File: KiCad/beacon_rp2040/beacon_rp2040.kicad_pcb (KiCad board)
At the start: 2 copper layers, 1 part, among them U1 RP2040-ZERO

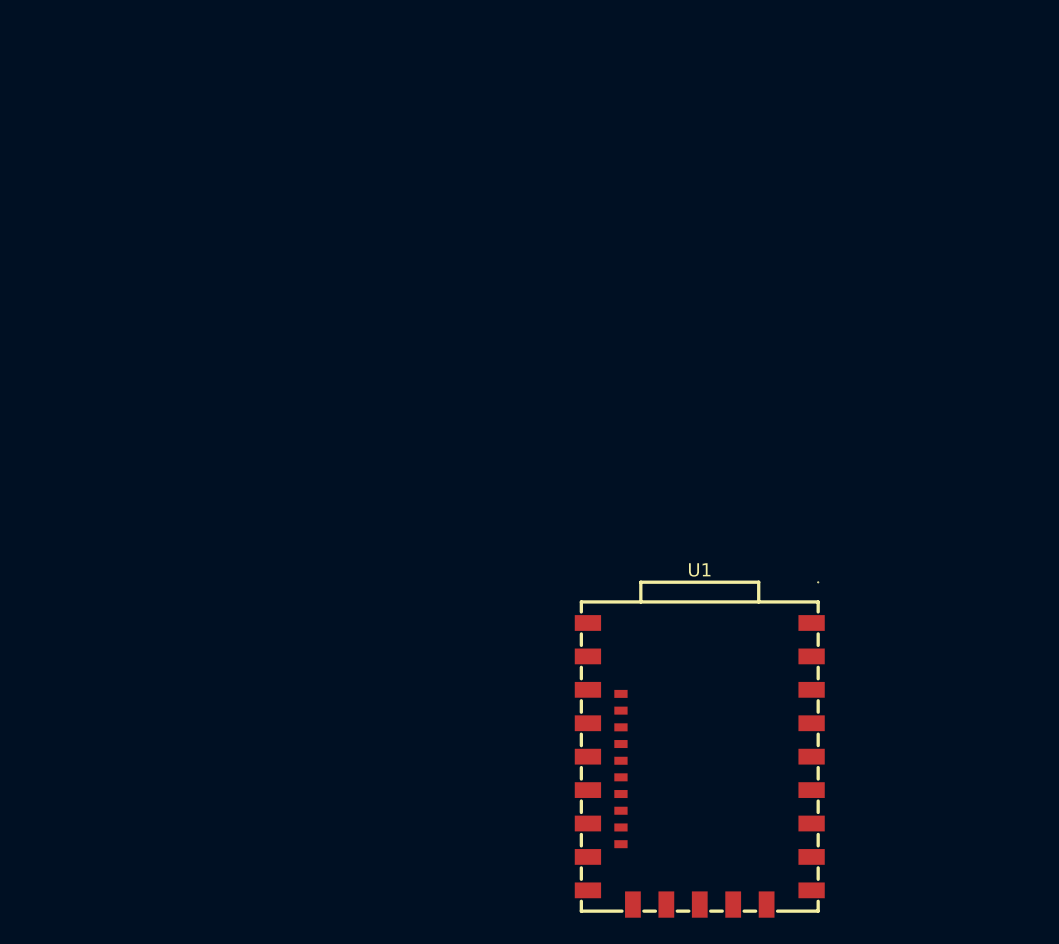
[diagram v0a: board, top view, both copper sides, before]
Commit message: Controller board: schematic, PCB, Gerbers, BOM; README hardware docs
- KiCad schematic and routed 2-layer PCB (75 x 32 mm): LM7805 supply
  with reverse-polarity and USB isolation diodes, audio attenuator with
  low-pass filter, BC817 open-collector PTT/CW outputs, Vin divider on
  GP26, GPIO/5V/GND expansion headers, M3 mounting holes
- Schematic PDF, Gerber + drill files (also zipped), interactive BOM
- Schematic and 3D view images in pics/
- README: board description, J1 pinout, outputs, power, expansion
  headers, manufacturing files and BOM; GUI download is now the zip
- VS Code CMake Tools builds into code/Beacon/build like the scripts

Co-Authored-By: Claude Opus 5.5 <noreply@anthropic.com>
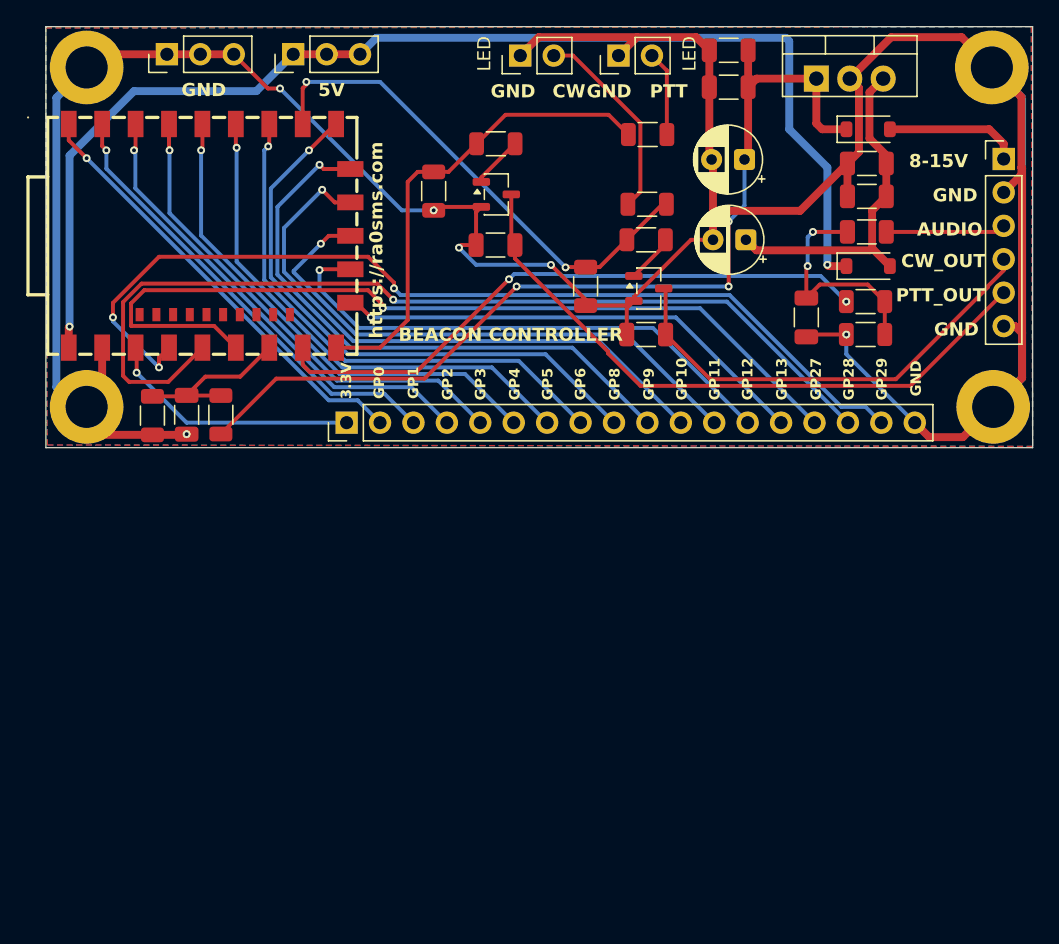
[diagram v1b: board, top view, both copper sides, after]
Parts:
- added C10: 100n, Capacitor_SMD:C_1206_3216Metric, F.Cu at (119.8, 36.2)
- added C11: 100n, Capacitor_SMD:C_1206_3216Metric, F.Cu at (130.3, 44.5)
- added C12: 10u, Capacitor_SMD:C_1206_3216Metric, F.Cu at (130.3, 42.0)
- added C13: 47uF, Capacitor_THT:CP_Radial_D5.0mm_P2.50mm, F.Cu at (121.1, 47.8)
- added C14: 47uF, Capacitor_THT:CP_Radial_D5.0mm_P2.50mm, F.Cu at (121.0, 41.7)
- added C2: 100n, Capacitor_SMD:C_1206_3216Metric, F.Cu at (113.5, 55.0)
- added C3: 100n, Capacitor_SMD:C_1206_3216Metric, F.Cu at (102.1, 48.2)
- added C4: 10u, Capacitor_SMD:C_1206_3216Metric, F.Cu at (130.3, 47.2)
- added C5: 100n, Capacitor_SMD:C_1206_3216Metric, F.Cu at (78.6, 61.1)
- added C6: 47n, Capacitor_SMD:C_1206_3216Metric, F.Cu at (125.7, 53.7)
- added C9: 10u, Capacitor_SMD:C_1206_3216Metric, F.Cu at (119.8, 33.4)
- added D1: MBR0540, Diode_SMD:D_SOD-123, F.Cu at (130.4, 49.8)
- added D2: LED_CW, Connector_PinHeader_2.54mm:PinHeader_1x02_P2.54mm_Vertical, F.Cu at (104.0, 33.8)
- added D3: LED_PTT, Connector_PinHeader_2.54mm:PinHeader_1x02_P2.54mm_Vertical, F.Cu at (111.4, 33.8)
- added D4: MBR0540, Diode_SMD:D_SOD-123, F.Cu at (130.4, 39.4)
- added H1: MountingHole_Pad, MountingHole:MountingHole_3.2mm_M3_DIN965_Pad, F.Cu at (71.0, 60.5)
- added H2: MountingHole_Pad, MountingHole:MountingHole_3.2mm_M3_DIN965_Pad, F.Cu at (139.9, 60.5)
- added H3: MountingHole_Pad, MountingHole:MountingHole_3.2mm_M3_DIN965_Pad, F.Cu at (139.8, 34.7)
- added H4: MountingHole_Pad, MountingHole:MountingHole_3.2mm_M3_DIN965_Pad, F.Cu at (71.0, 34.7)
- added J1: CONNECTIONS, Connector_PinHeader_2.54mm:PinHeader_1x06_P2.54mm_Vertical, F.Cu at (140.7, 41.7)
- added J2: GPIOs, Connector_PinHeader_2.54mm:PinHeader_1x18_P2.54mm_Vertical, F.Cu at (90.8, 61.7)
- added J3: GND, Connector_PinHeader_2.54mm:PinHeader_1x03_P2.54mm_Vertical, F.Cu at (77.1, 33.7)
- added J4: 5V, Connector_PinHeader_2.54mm:PinHeader_1x03_P2.54mm_Vertical, F.Cu at (86.7, 33.7)
- added Q3: BC817, Package_TO_SOT_SMD:SOT-23-3, F.Cu at (102.1, 44.4)
- added Q4: BC817, Package_TO_SOT_SMD:SOT-23-3, F.Cu at (113.7, 51.5)
- added R1: 34k, Resistor_SMD:R_1206_3216Metric, F.Cu at (130.2, 52.5)
- added R10: 1k, Resistor_SMD:R_1206_3216Metric, F.Cu at (102.1, 40.5)
- added R2: 1k, Resistor_SMD:R_1206_3216Metric, F.Cu at (130.2, 55.0)
- added R3: 10k, Resistor_SMD:R_1206_3216Metric, F.Cu at (108.9, 51.3)
- added R4: 1k, Resistor_SMD:R_1206_3216Metric, F.Cu at (113.6, 45.1)
- added R5: 10k, Resistor_SMD:R_1206_3216Metric, F.Cu at (97.4, 44.1)
- added R6: 1k, Resistor_SMD:R_1206_3216Metric, F.Cu at (113.6, 39.8)
- added R7: 100k, Resistor_SMD:R_1206_3216Metric, F.Cu at (81.2, 61.1)
- added R8: 10k, Resistor_SMD:R_1206_3216Metric, F.Cu at (76.0, 61.2)
- added R9: 1k, Resistor_SMD:R_1206_3216Metric, F.Cu at (113.5, 47.8)
- added U2: LM7805_TO220, Package_TO_SOT_THT:TO-220-3_Vertical, F.Cu at (126.5, 35.5)
- moved U1 54.8 mm to (80.3, 47.5), turned to 90 degrees
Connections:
- U1 pad 1: unconnected-(U1-GP0-Pad1) -> GP0
- U1 pad 10: unconnected-(U1-GP9-Pad10) -> GP9
- U1 pad 11: unconnected-(U1-GP10-Pad11) -> GP10
- U1 pad 12: unconnected-(U1-GP11-Pad12) -> GP11
- U1 pad 13: unconnected-(U1-GP12-Pad13) -> GP12
- U1 pad 14: unconnected-(U1-GP13-Pad14) -> GP13
- U1 pad 15: unconnected-(U1-GP14-Pad15) -> PTT
- U1 pad 16: unconnected-(U1-GP15-Pad16) -> Net-(U1-GP15)
- U1 pad 17: unconnected-(U1-GP26-Pad17) -> Net-(U1-GP26)
- U1 pad 18: unconnected-(U1-GP27-Pad18) -> GP27
- U1 pad 19: unconnected-(U1-GP28-Pad19) -> GP28
- U1 pad 2: unconnected-(U1-GP1-Pad2) -> GP1
- U1 pad 20: unconnected-(U1-GP29-Pad20) -> GP29
- U1 pad 21: unconnected-(U1-3V3-Pad21) -> 3.3V
- U1 pad 22: unconnected-(U1-GND-Pad22) -> GND
- U1 pad 23: unconnected-(U1-5V-Pad23) -> +5V
- U1 pad 3: unconnected-(U1-GP2-Pad3) -> GP2
- U1 pad 4: unconnected-(U1-GP3-Pad4) -> GP3
- U1 pad 5: unconnected-(U1-GP4-Pad5) -> GP4
- U1 pad 6: unconnected-(U1-GP5-Pad6) -> GP5
- U1 pad 7: unconnected-(U1-GP6-Pad7) -> GP6
- U1 pad 8: unconnected-(U1-GP7-Pad8) -> CW
- U1 pad 9: unconnected-(U1-GP8-Pad9) -> GP8
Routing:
- net GND: track 0.00 -> 253.5 mm, vias 0 -> 6
- net +5V: track 0.00 -> 92.8 mm, vias 0 -> 2
- net GP29: track 0.00 -> 73.5 mm, vias 0 -> 3
- net Net-(D4-K): track 0.00 -> 73.1 mm, vias 0 -> 3
- net GP28: track 0.00 -> 73.0 mm, vias 0 -> 1
- net GP27: track 0.00 -> 67.0 mm, vias 0 -> 1
- net Net-(J1-Pin_5): track 0.00 -> 49.2 mm
- net Net-(U1-GP15): track 0.00 -> 46.8 mm, vias 0 -> 2
- net GP9: track 0.00 -> 44.9 mm, vias 0 -> 1
- net GP10: track 0.00 -> 44.9 mm, vias 0 -> 1
- net GP8: track 0.00 -> 44.4 mm, vias 0 -> 1
- net GP11: track 0.00 -> 42.2 mm, vias 0 -> 1
- net GP6: track 0.00 -> 40.5 mm, vias 0 -> 1
- net GP12: track 0.00 -> 40.5 mm, vias 0 -> 1
- net GP5: track 0.00 -> 39.2 mm, vias 0 -> 1
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- added copper zone on B.Cu, net GND
- added copper zone on F.Cu, net GND
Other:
- board outline added: 75 x 32 mm
- board text added: "3.3V"
- board text added: "5V"
- board text added: "8-15V"
- board text added: "AUDIO"
- board text added: "BEACON CONTROLLER"
- board text added: "CW"
- board text added: "CW_OUT"
- board text added: "GND"
- board text added: "GP0"
- board text added: "GP1"
- board text added: "GP10"
- board text added: "GP11"
- board text added: "GP12"
- board text added: "GP13"
- board text added: "GP2"
- board text added: "GP27"
- board text added: "GP28"
- board text added: "GP29"
- board text added: "GP3"
- board text added: "GP4"
- board text added: "GP5"
- board text added: "GP6"
- board text added: "GP8"
- board text added: "GP9"
- board text added: "LED"
- board text added: "PTT"
- board text added: "PTT_OUT"
- board text added: "https://ra0sms.com"
